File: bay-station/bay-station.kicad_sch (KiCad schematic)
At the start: 0 parts

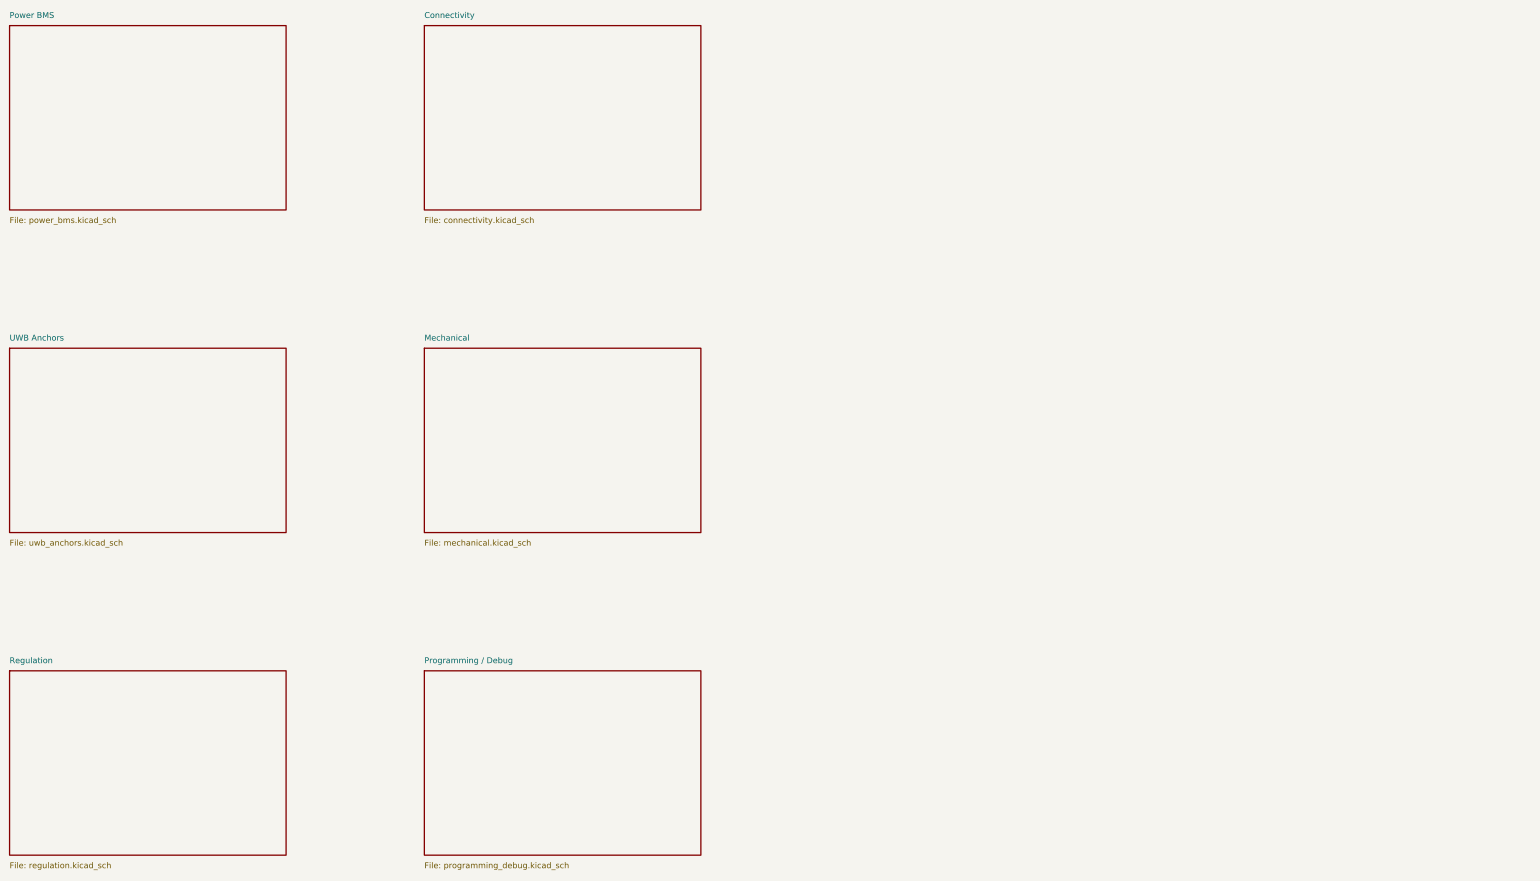
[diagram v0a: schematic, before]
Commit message: Bay station: discrete DW3210 array on a shared clock, Nordic BT840 host
Two coupled changes, both forced by the positioning scheme.

UWB ARRAY. TDoA compares timestamps across receivers, so they must share a
time base. The DWM3000 module makes that impossible -- its 24 pins contain
no clock pin and its crystal is internal and unreachable, so four of them
cannot be synchronised at any price. The bare DW3000 IC can: Datasheet v1.3
Table 10 states a 38.4 MHz signal may be supplied from an external reference
via the XTI overdrive pin. Four DW3210s (QFN40, not the 52-ball WLCSP
DW3110 the module is built on) now sit on one PCB sharing one TCXO through
a 1:4 low-skew buffer, with the antennas remote on ~1-2 m SMA coax. This
makes synchronisation structurally absent rather than solved.

uwb_anchors.kicad_sch renamed to uwb_array.kicad_sch -- the four receivers
are one on-board array, not distributed anchor units. U4 is A0, the CENTER
anchor; U5-U7 are A1-A3 outer. They are not interchangeable peers.

New clock_dist.kicad_sch holds the shared reference network. Placed are only
the passives the datasheet actually specifies: 2200 pF AC coupling into each
XTI and 1 pF from each XTO to ground, both required only because an external
clock is used. TCXO and buffer parts are not yet selected.

HOST MCU. The uplink moved from WiFi-to-internet to BLE-to-a-laptop, and
WiFi was the only thing keeping this board off Nordic. ESP32-S3-WROOM-1 is
replaced by a Fanstel BT840 (nRF52840), which gives one toolchain across
both boards and aligns with Qorvo's DW3000 reference stack -- easing the
multi-instance driver work that sits on the critical path. Note the
ESP32-S3 is BLE-only with no Classic/SPP, so the laptop link is a GATT
service.

programming_debug collapsed accordingly: Nordic programs over SWD, so the
boot straps, EN RC delay, BOOT button and the data-capable USB-C are gone,
replaced by a 2x5 ARM Cortex Debug header. That RESOLVES the long-standing
two-USB-C open item by deletion -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
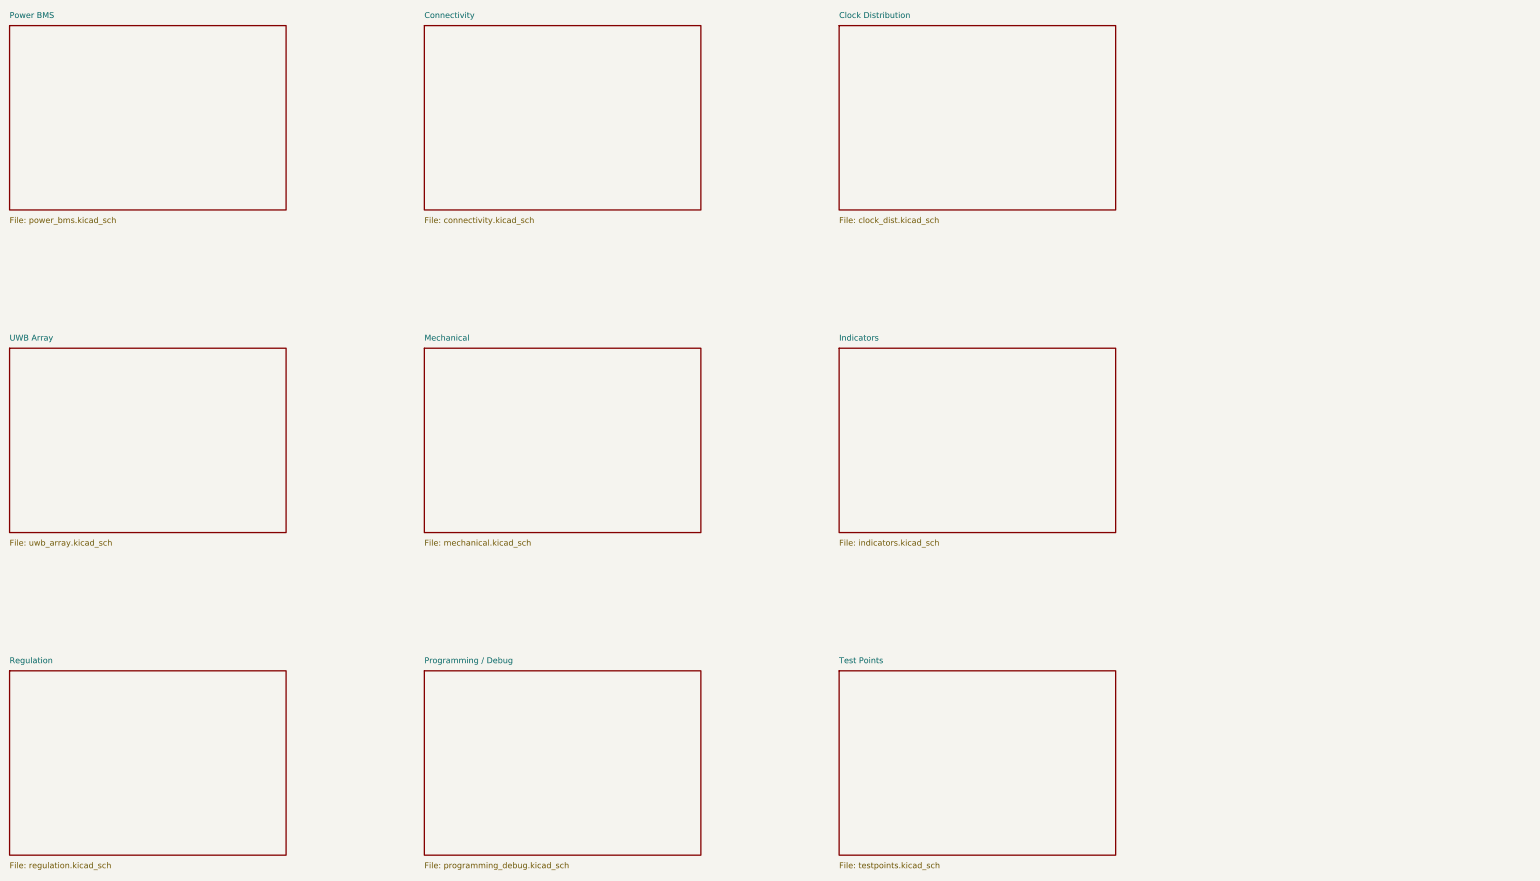
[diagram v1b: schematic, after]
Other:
- sheet UWB Anchors renamed UWB Array
- added sheet Clock Distribution (clock_dist.kicad_sch)
- added sheet Indicators (indicators.kicad_sch)
- added sheet Test Points (testpoints.kicad_sch)
- sheet UWB Array: file uwb_anchors.kicad_sch -> uwb_array.kicad_sch
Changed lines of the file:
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@@
 			(color 0 0 0 0)
 		)
-		(property "Sheetname" "UWB Anchors"
+		(property "Sheetname" "UWB Array"
 			(at 30 98.5 0)
 			(show_name no)
@@
 			)
 		)
-		(property "Sheetfile" "uwb_anchors.kicad_sch"
+		(property "Sheetfile" "uwb_array.kicad_sch"
 			(at 30 141.5 0)
 			(show_name no)
@@
 				)
 			)
+		)
+	)
+	(sheet
+		(at 210 30)
+		(size 60 40)
+		(fields_autoplaced yes)
+		(stroke
+			(width 0.1524)
+			(type solid)
+		)
+		(fill
+			(color 0 0 0 0.0000)
+		)
+		(property "Sheetname" "Clock Distribution"
+			(at 210 28.5 0)
+			(effects
+				(font
+					(size 1.27 1.27)
+				)
+				(justify left bottom)
+			)
+		)
+		(property "Sheetfile" "clock_dist.kicad_sch"
+			(at 210 71.5 0)
+			(effects
+				(font
+					(size 1.27 1.27)
+				)
+				(justify left top)
+			)
+		)
+		(instances
+			(project "bay-station"
+				(path "/543ba435-6cf4-448c-821e-3c5778b02e9c"
+					(page "8")
+				)
+			)
+		)
+	)
+	(sheet
+		(at 210 100)
+		(size 60 40)
+		(fields_autoplaced yes)
+		(stroke
+			(width 0.1524)
+			(type solid)
+		)
+		(fill
+			(color 0 0 0 0.0000)
+		)
+		(property "Sheetname" "Indicators"
+			(at 210 98.5 0)
+			(effects
+				(font
+					(size 1.27 1.27)
+				)
+				(justify left bottom)
+			)
+		)
+		(property "Sheetfile" "indicators.kicad_sch"
+			(at 210 141.5 0)
+			(effects
+				(font
+					(size 1.27 1.27)
+				)
+				(justify left top)
+			)
+		)
+		(instances
+			(project "bay-station"
+				(path "/543ba435-6cf4-448c-821e-3c5778b02e9c"
+					(page "9")
+				)
+			)
+		)
+	)
+	(sheet
+		(at 210 170)
+		(size 60 40)
+		(fields_autoplaced yes)
+		(stroke
+			(width 0.1524)
+			(type solid)
+		)
+		(fill
+			(color 0 0 0 0.0000)
+		)
+		(property "Sheetname" "Test Points"
+			(at 210 168.5 0)
+			(effects
+				(font
+					(size 1.27 1.27)
+				)
+				(justify left bottom)
+			)
+		)
+		(property "Sheetfile" "testpoints.kicad_sch"
+			(at 210 211.5 0)
+			(effects
+				(font
+					(size 1.27 1.27)
+				)
+				(justify left top)
+			)
+		)
+		(instances
+			(project "bay-station"
+				(path "/543ba435-6cf4-448c-821e-3c5778b02e9c"
+					(page "9")
+				)
+			)

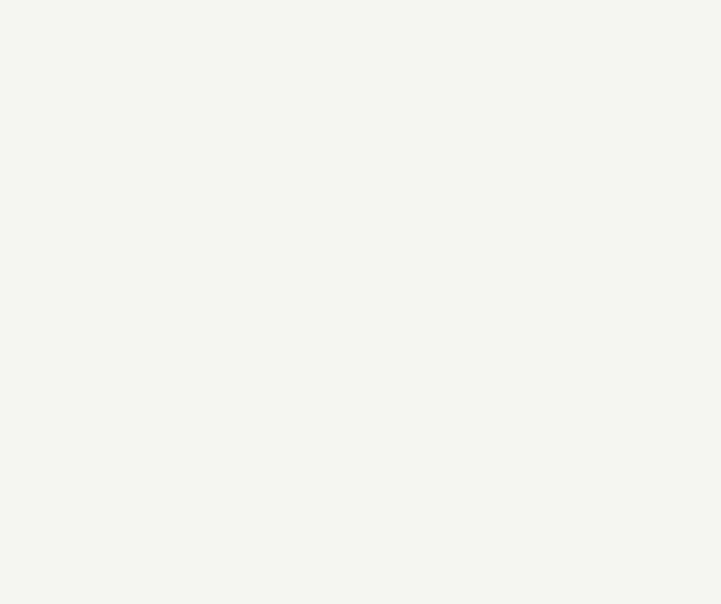
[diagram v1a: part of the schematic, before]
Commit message: Georeference the bay station: GNSS, magnetometer, tilt sensor
The station is deployed outdoors and moved between sites, and the UWB
array only ever produced position RELATIVE to its own antenna frame --
usable by an operator standing at it, useless as a coordinate to hand
anyone else.

Position alone would not have fixed that. A GNSS fix says where the
station is, not which way it faces, and the array reports bearing
relative to the frame -- so without heading you get a circle of possible
tag locations, not a point. Hence three parts on the new gnss sheet:

  U9  u-blox MAX-M10S  -- where the station is
  U10 ST LIS3MDL       -- which way it faces
  U11 ST LIS2DH        -- tilt compensation for U10, since a magnetometer
                          only reads heading correctly when level and this
                          station is set down on varying terrain. Also
                          detects the station being knocked, which silently
                          invalidates both the fix and the heading.

All three are KiCad stock symbols AND footprints, deliberately: the board
already carries two outstanding vendor-footprint imports (BT840, and
DWM3001C on the tag) and a third was not worth taking on. SAM-M10Q with
its integrated patch antenna was the alternative and would have deleted
the antenna line entirely, but KiCad has neither symbol nor footprint for
it.

U9 pin data verified against the real u-blox Data Sheet UBX-20035208 R02,
Table 9: 17 of 18 pins match KiCad's symbol. Pin 15 does not -- "Reserved"
in R02, VIO_SEL in KiCad, most likely a later revision. Left open, flagged
on the sheet and in decisions.md. Datasheet also requires VCC (8) and V_IO
(7) tied together and SAFEBOOT_N (18) left open; both recorded.

Accuracy recorded rather than glossed: uncorrected GNSS is 2-5 m against
the array's 10-30 cm, so the world-frame anchor is 10-30x coarser than the
relative fix hanging off it. Host-side survey-in averaging narrows it to
sub-metre, but restarts at e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
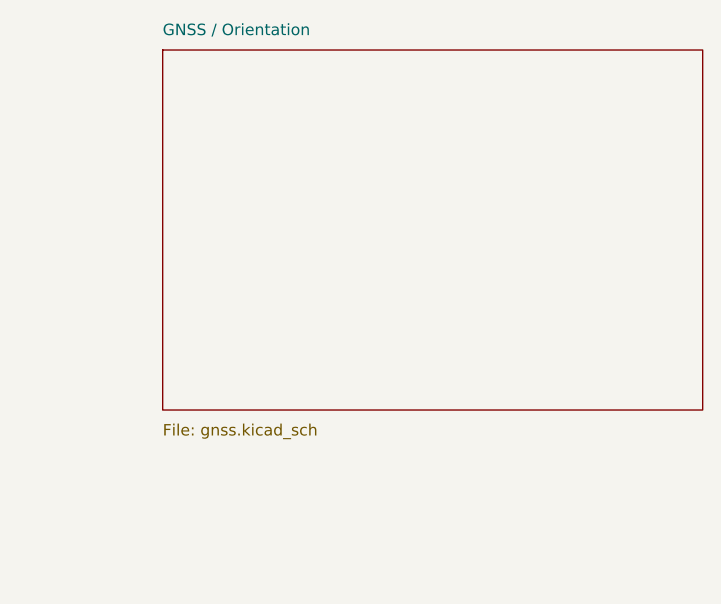
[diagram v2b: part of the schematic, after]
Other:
- added sheet GNSS / Orientation (gnss.kicad_sch)
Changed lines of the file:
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@@
+		)
+	)
+	(sheet
+		(at 300 30)
+		(size 60 40)
+		(fields_autoplaced yes)
+		(stroke
+			(width 0.1524)
+			(type solid)
+		)
+		(fill
+			(color 0 0 0 0.0000)
+		)
+		(property "Sheetname" "GNSS / Orientation"
+			(at 300 28.5 0)
+			(effects
+				(font
+					(size 1.27 1.27)
+				)
+				(justify left bottom)
+			)
+		)
+		(property "Sheetfile" "gnss.kicad_sch"
+			(at 300 71.5 0)
+			(effects
+				(font
+					(size 1.27 1.27)
+				)
+				(justify left top)
+			)
+		)
+		(instances
+			(project "bay-station"
+				(path "/543ba435-6cf4-448c-821e-3c5778b02e9c"
+					(page "10")
+				)
+			)
 		)
 	)

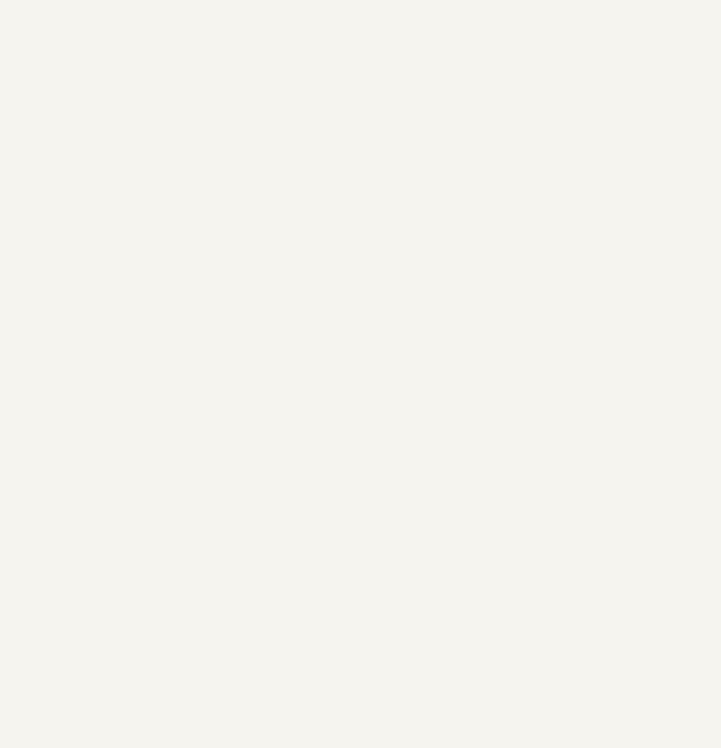
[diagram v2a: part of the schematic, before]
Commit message: Add a dual-band Wi-Fi uplink as an SPI co-processor, not a host swap
New sheet `bay-station/wifi.kicad_sch` (page 11): ESP32-C5-WROOM-1 (U12)
plus C37/C38, placement only, matching the rest of this board.

GNSS was already done -- gnss.kicad_sch has carried a u-blox MAX-M10S since
2026-09-23, so nothing was added there.

Why a co-processor. The nRF52840 cannot host a Wi-Fi stack alongside this
application. Nordic's own memory tables, measured on an nRF52840 DK, give
station mode at 224 KB RAM and an MQTT sample at 384 KB, against 256 KB
total on the part. Station mode alone would leave ~32 KB for the BLE stack,
the four-instance DW3210 driver and the position solve. The ESP32-C5 runs
Wi-Fi and TCP/IP itself, so the host cost is a transport driver.

This does NOT revert the 2026-09-19 decision that removed the ESP32-S3. That
call was about the ESP32 as *host*; here it is an SPI peripheral and the
BT840 remains the host.

Ruled out deliberately:
- Wi-Fi 6E / any 6 GHz part. 5925-7125 MHz sits directly on top of UWB
  channel 5 at 6489.6 MHz -- a co-located transmitter inside the receive
  band of a design where 1 ns is 30 cm.
- Nordic nRF7002. Good silicon (SPI/QSPI, IOVDD 1.62-3.6 V so no level
  shifting, BLE coex interface) but it is a radio companion, not a stack
  companion -- the Wi-Fi stack still lands on the host, which is the one
  thing the nRF52840 cannot afford. Also needs a diplexer or two antennas.

GPIO: the answer to "will we run out" is no. 33 of 48 allocated across the
UWB array, Wi-Fi, GNSS, sensors, clock, indicators, debug and test points --
15 spare. Full table in docs/decisions.md. No expander, and one should not
be added: it would sit in the DW3210 CS/IRQ path. The real constraint is
peripheral assignment, not pin count -- the DW3210 bus needs the fast SPIM
instance and Wi-Fi must be on a different one so it cannot stall an
exchange.

Verified against Espressif ESP32-C5-WROOM-1 & WROOM-1U Datasheet v1.3:
29 pins from Table 3-1 (both pdftotext m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
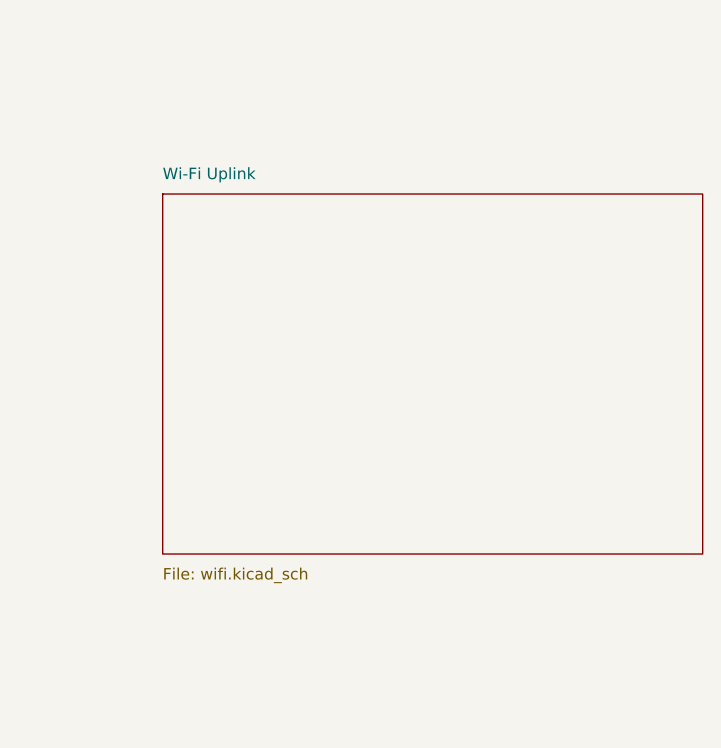
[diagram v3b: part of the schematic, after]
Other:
- added sheet Wi-Fi Uplink (wifi.kicad_sch)
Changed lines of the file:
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@@
+		)
+	)
+	(sheet
+		(at 300 100)
+		(size 60 40)
+		(fields_autoplaced yes)
+		(stroke
+			(width 0.1524)
+			(type solid)
+		)
+		(fill
+			(color 0 0 0 0.0000)
+		)
+		(property "Sheetname" "Wi-Fi Uplink"
+			(at 300 98.5 0)
+			(effects
+				(font
+					(size 1.27 1.27)
+				)
+				(justify left bottom)
+			)
+		)
+		(property "Sheetfile" "wifi.kicad_sch"
+			(at 300 141.5 0)
+			(effects
+				(font
+					(size 1.27 1.27)
+				)
+				(justify left top)
+			)
+		)
+		(instances
+			(project "bay-station"
+				(path "/543ba435-6cf4-448c-821e-3c5778b02e9c"
+					(page "11")
+				)
+			)
 		)
 	)
